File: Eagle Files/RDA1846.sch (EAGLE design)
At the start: 1 part

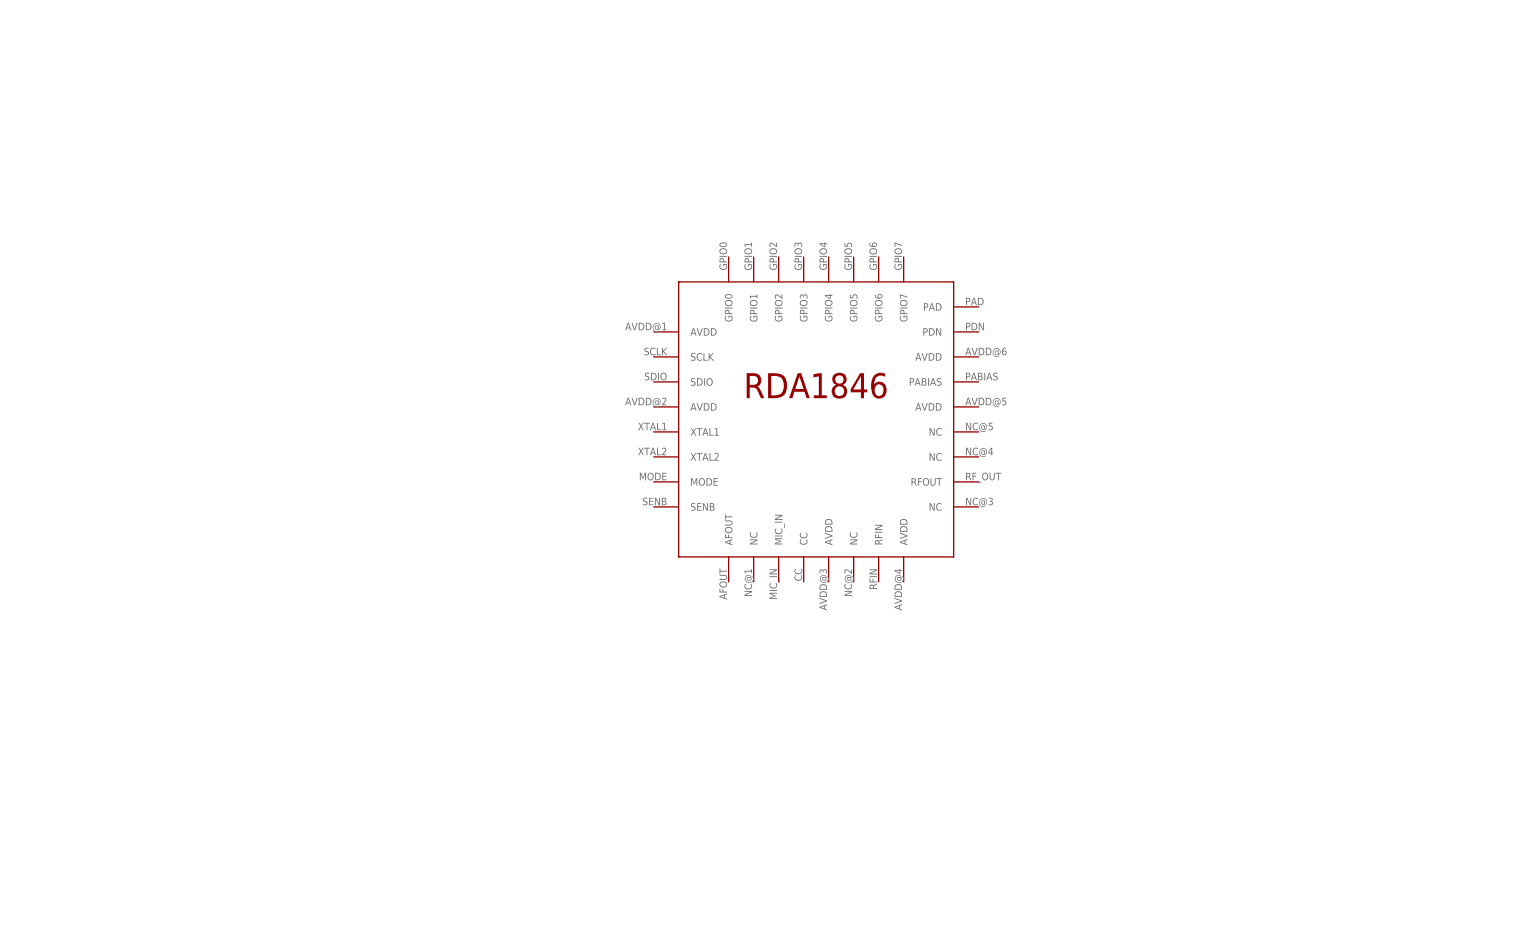
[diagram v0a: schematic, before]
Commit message: Added FA-128 XTAL Library. WIP : Schematic
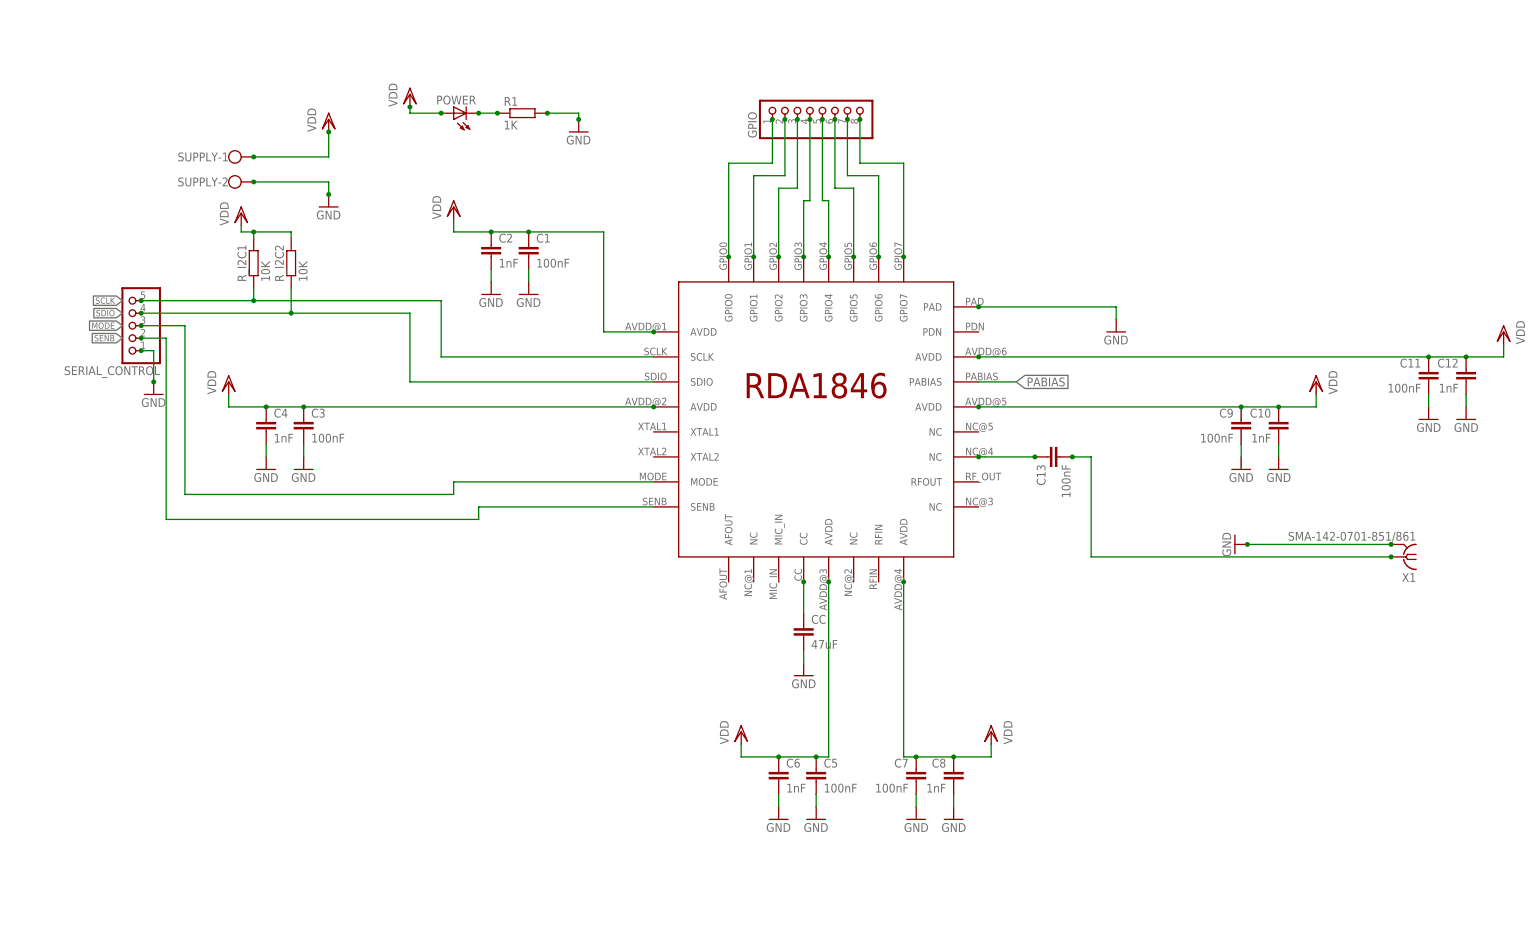
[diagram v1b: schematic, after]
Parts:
- added C1, C11, C13, C3, C5, C7, C9: 100nF, rcl:C-EUC0805
- added C10, C12, C2, C4, C6, C8: 1nF, rcl:C-EUC0805
- added CC: 47uF, rcl:C-EUC0805
- added GPIO: (no value), adafruit:PINHD-1X8CLEANBIG
- added POWER: (no value), adafruit:LEDCHIPLED_1206
- added R1: 1K, rcl:R-EU_R0805
- added R_I2C1, R_I2C2: 10K, rcl:R-EU_R0805
- added SERIAL_CONTROL: (no value), pinhead:PINHD-1X5
- added SUPPLY: (no value), con-wago-500:W237-102
- added X1: SMA-142-0701-851/861, con-coax:SMA-142-0701-851/861
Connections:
- new net GND: C1.2, C10.2, C11.2, C12.2, C2.2, C3.2, C4.2, C5.2, C6.2, C7.2, C8.2, C9.2, CC.2, R1.2, SERIAL_CONTROL.1, SUPPLY-2.KL, U$1.PAD, X1.2
- new net MODE: SERIAL_CONTROL.3, U$1.MODE
- new net N$1: GPIO.1, U$1.GPIO0
- new net N$10: CC.1, U$1.CC
- new net N$11: C13.1, U$1.NC@4
- new net N$12: C13.2, X1.1
- new net N$2: GPIO.8, U$1.GPIO7
- new net N$3: GPIO.2, U$1.GPIO1
- new net N$4: GPIO.7, U$1.GPIO6
- new net N$5: GPIO.3, U$1.GPIO2
- new net N$6: GPIO.6, U$1.GPIO5
- new net N$7: GPIO.4, U$1.GPIO3
- new net N$8: GPIO.5, U$1.GPIO4
- new net N$9: POWER.C, R1.1
- new net PABIAS: U$1.PABIAS
- new net SCLK: R_I2C1.1, SERIAL_CONTROL.5, U$1.SCLK
- new net SDIO: R_I2C2.1, SERIAL_CONTROL.4, U$1.SDIO
- new net SENB: SERIAL_CONTROL.2, U$1.SENB
- new net VDD: C1.1, C10.1, C11.1, C12.1, C2.1, C3.1, C4.1, C5.1, C6.1, C7.1, C8.1, C9.1, POWER.A, R_I2C1.2, R_I2C2.2, SUPPLY-1.KL, U$1.AVDD@1, U$1.AVDD@2, U$1.AVDD@3, U$1.AVDD@4, U$1.AVDD@5, U$1.AVDD@6

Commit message: Schematics done. Layout WIP. Check RF Switch dimensions
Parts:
- added AOUT, MIC: (no value), pinhead:PINHD-1X2
- added C14, C15: 9pF, rcl:C-EUC0805
- added C16, C17: 47uF, rcl:C-EUC0805
- added C18, C19, C20: (no value), rcl:C-USC1206
- added ENABLE, RF_SWITCH: (no value), pinhead:PINHD-1X3
- added PABIAS: (no value), con-wago-500:W237-102
- added RFIN, RFOUT: SMA-142-0701-851/861, con-coax:SMA-142-0701-851/861
- added U$2: CRYSTAL_FA_128, FA_128:CRYSTAL_FA_128
- added U$3: RF_SWITCH, RF_SWITCH:RF_SWITCH
- added X2, X3: SMA-142-0701-871/876, con-coax:SMA-142-0701-871/876
- X1: value SMA-142-0701-851/861 -> SMA-142-0701-871/876; device con-coax:SMA-142-0701-851/861 -> con-coax:SMA-142-0701-871/876
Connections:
- new net N$13: C15.1, U$1.XTAL1, U$2.OP1
- new net N$14: C14.1, U$1.XTAL2, U$2.OP2
- new net N$15: C16.2, U$1.AFOUT
- new net N$16: C17.2, U$1.MIC_IN
- new net N$17: AOUT.2, C16.1
- new net N$18: C17.1, MIC.2
- new net N$19: RFIN.1, U$1.RFIN
- new net N$20: C19.2, X1.1
- new net N$21: C19.1, U$3.J3
- new net N$22: C20.1, U$3.J2
- new net N$23: C20.2, X2.1
- new net N$24: C18.1, U$3.RF
- new net N$25: C18.2, X3.1
- new net N$26: RF_SWITCH.2, U$3.V2
- new net N$27: RF_SWITCH.3, U$3.V1
- new net PDN: ENABLE.2, U$1.PDN
- net GND: now also AOUT.1, C14.2, C15.2, ENABLE.1, MIC.1, PABIAS-2.KL, RFIN.2, RFOUT.2, RF_SWITCH.1, U$2.GND, U$2.GND_1, U$3.GND, X2.2
- net N$11: now also U$1.RFOUT; no longer U$1.NC@4
- net N$12: now also RFOUT.1; no longer X1.1
- net PABIAS: now also PABIAS-1.KL
- net VDD: now also ENABLE.3

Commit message: Placing of component done. Removed demod spec due to size constraints
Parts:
- removed AOUT: (no value), pinhead:PINHD-1X2
- removed C16: 47uF, rcl:C-EUC0805
- removed PABIAS: (no value), con-wago-500:W237-102
- removed RFIN: SMA-142-0701-851/861, con-coax:SMA-142-0701-851/861
- removed RF_SWITCH: (no value), pinhead:PINHD-1X3
- removed SERIAL_CONTROL: (no value), pinhead:PINHD-1X5
- added JP1: (no value), pinhead:PINHD-1X2
- added JP2, JP3: (no value), pinhead:PINHD-1X3
- added JP4, JP5, JP6: (no value), pinhead:PINHD-1X1
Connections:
- removed net N$15: C16.2, U$1.AFOUT
- removed net N$17: AOUT.2, C16.1
- removed net N$19: RFIN.1, U$1.RFIN
- net GND: now also JP1.1, JP2.1, JP3.1, JP4.1, SUPPLY-1.KL; no longer AOUT.1, PABIAS-2.KL, RFIN.2, RF_SWITCH.1, SERIAL_CONTROL.1, SUPPLY-2.KL
- net MODE: now also JP3.3; no longer SERIAL_CONTROL.3
- net N$26: now also JP5.1; no longer RF_SWITCH.2
- net N$27: now also JP6.1; no longer RF_SWITCH.3
- net PABIAS: now also JP1.2; no longer PABIAS-1.KL
- net SCLK: now also JP2.3; no longer SERIAL_CONTROL.5
- net SDIO: now also JP2.2; no longer SERIAL_CONTROL.4
- net SENB: now also JP3.2; no longer SERIAL_CONTROL.2
- net VDD: now also SUPPLY-2.KL; no longer SUPPLY-1.KL

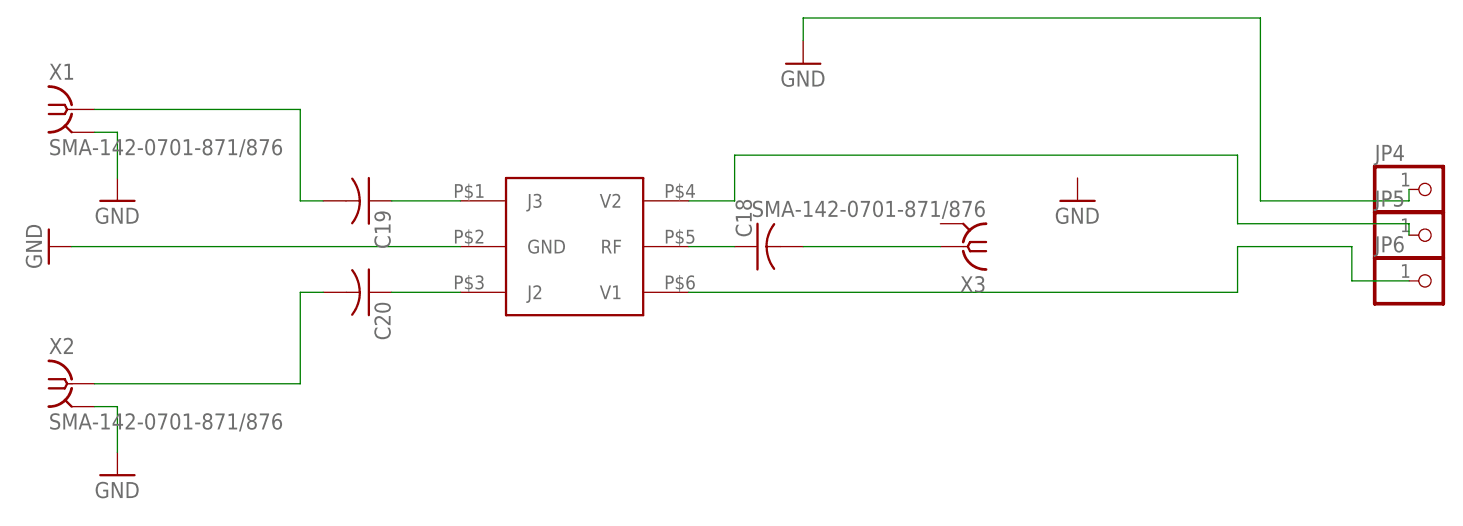
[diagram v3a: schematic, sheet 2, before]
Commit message: Layout RDA almost done. VCC lines remaining
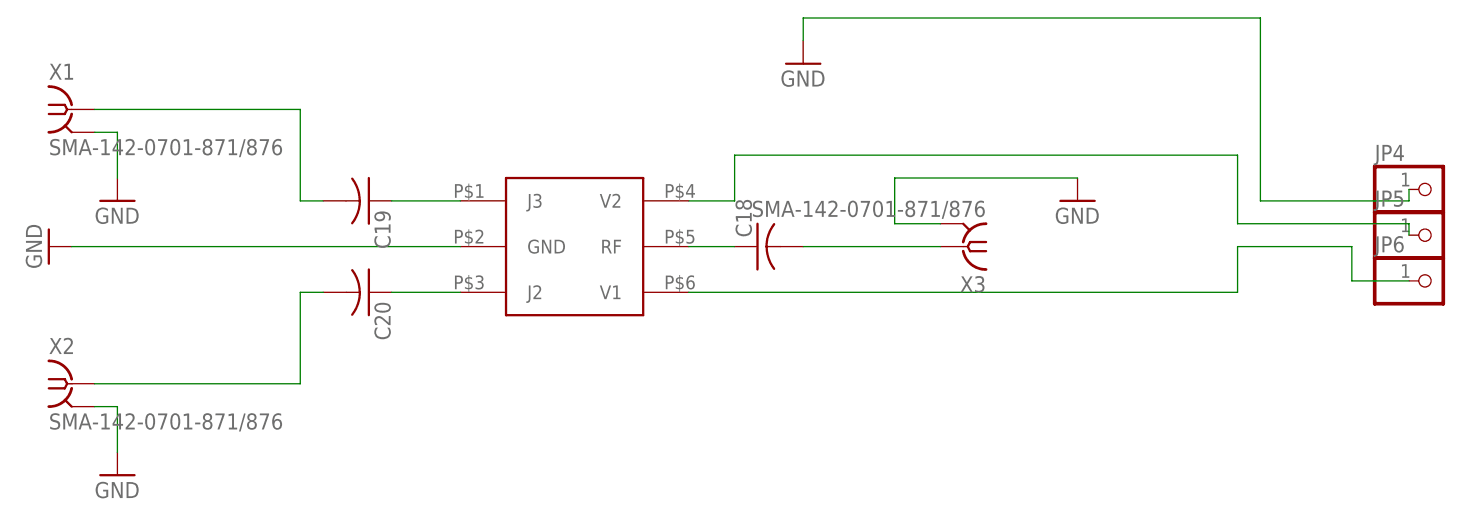
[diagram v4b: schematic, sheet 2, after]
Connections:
- net GND: now also X3.2
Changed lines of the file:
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@@
 <setting verticaltext="up"/>
 </settings>
-<grid distance="50" unitdist="mil" unit="mil" style="lines" multiple="1" display="no" altdistance="0.01" altunitdist="inch" altunit="inch"/>
+<grid distance="0.1" unitdist="inch" unit="inch" style="lines" multiple="1" display="no" altdistance="0.01" altunitdist="inch" altunit="inch"/>
 <layers>
 <layer number="1" name="Top" color="4" fill="1" visible="no" active="no"/>
@@
 <wire x1="156.21" y1="63.5" x2="156.21" y2="64.77" width="0.1524" layer="91"/>
 </segment>
-</net>
+<segment>
+<pinref part="X3" gate="G1" pin="2"/>
+<wire x1="104.14" y1="60.96" x2="99.06" y2="60.96" width="0.1524" layer="91"/>
+<wire x1="99.06" y1="60.96" x2="99.06" y2="66.04" width="0.1524" layer="91"/>
+<pinref part="GND31" gate="1" pin="GND"/>
+<wire x1="99.06" y1="66.04" x2="119.38" y2="66.04" width="0.1524" layer="91"/>
+</segment>
+</net>

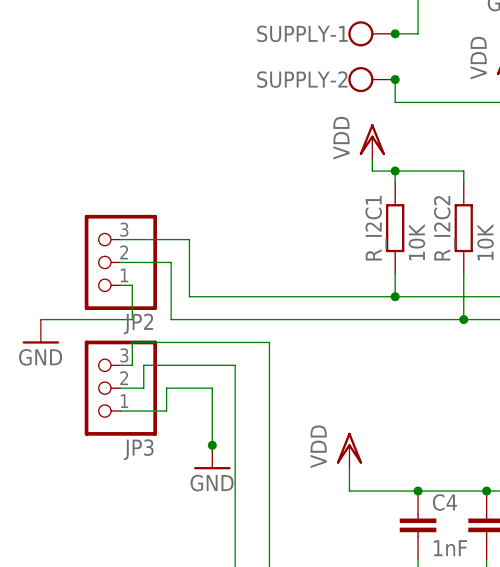
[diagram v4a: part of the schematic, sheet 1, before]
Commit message: Completed layout and routing. Need to adjust labels and values
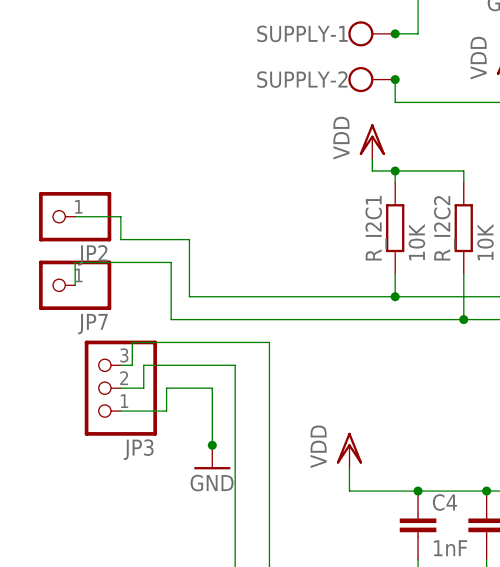
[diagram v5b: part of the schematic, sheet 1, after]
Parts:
- added JP7: (no value), adafruit:PINHD-1X1
- JP2: device pinhead:PINHD-1X3 -> adafruit:PINHD-1X1
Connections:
- net GND: no longer JP2.1
- net SCLK: now also JP2.1; no longer JP2.3
- net SDIO: now also JP7.1; no longer JP2.2
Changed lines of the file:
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@@
 <part name="GND31" library="supply1" deviceset="GND" device=""/>
 <part name="GND32" library="supply1" deviceset="GND" device=""/>
-<part name="JP2" library="pinhead" deviceset="PINHD-1X3" device=""/>
 <part name="JP3" library="pinhead" deviceset="PINHD-1X3" device=""/>
-<part name="GND33" library="supply1" deviceset="GND" device=""/>
 <part name="JP1" library="pinhead" deviceset="PINHD-1X2" device=""/>
 <part name="JP4" library="pinhead" deviceset="PINHD-1X1" device=""/>
 <part name="JP5" library="pinhead" deviceset="PINHD-1X1" device=""/>
 <part name="JP6" library="pinhead" deviceset="PINHD-1X1" device=""/>
+<part name="JP2" library="adafruit" deviceset="PINHD-1X1" device=""/>
+<part name="JP7" library="adafruit" deviceset="PINHD-1X1" device=""/>
 </parts>
 <sheets>
@@
 <instance part="GND26" gate="1" x="62.23" y="113.03"/>
 <instance part="VDD10" gate="G$1" x="62.23" y="128.27" rot="MR0"/>
-<instance part="JP2" gate="A" x="-132.08" y="76.2" rot="R180"/>
 <instance part="JP3" gate="A" x="-132.08" y="62.23" rot="R180"/>
-<instance part="GND33" gate="1" x="-138.43" y="67.31"/>
 <instance part="JP1" gate="G$1" x="68.58" y="97.79" rot="R180"/>
+<instance part="JP2" gate="G$1" x="-137.16" y="81.28" rot="R180"/>
+<instance part="JP7" gate="G$1" x="-137.16" y="73.66" rot="R180"/>
 </instances>
 <busses>
@@
 <junction x="-99.06" y="101.6"/>
 </segment>
-<segment>
-<pinref part="JP2" gate="A" pin="1"/>
-<wire x1="-129.54" y1="73.66" x2="-128.27" y2="73.66" width="0.1524" layer="91"/>
-<wire x1="-128.27" y1="73.66" x2="-128.27" y2="69.85" width="0.1524" layer="91"/>
-<pinref part="GND33" gate="1" pin="GND"/>
-<wire x1="-128.27" y1="69.85" x2="-138.43" y2="69.85" width="0.1524" layer="91"/>
-</segment>
 </net>
 <net name="PABIAS" class="0">
@@
 <junction x="-99.06" y="72.39"/>
 <wire x1="-121.92" y1="72.39" x2="-99.06" y2="72.39" width="0.1524" layer="91"/>
-<pinref part="JP2" gate="A" pin="3"/>
 <wire x1="-129.54" y1="78.74" x2="-121.92" y2="78.74" width="0.1524" layer="91"/>
 <wire x1="-121.92" y1="78.74" x2="-121.92" y2="72.39" width="0.1524" layer="91"/>
+<pinref part="JP2" gate="G$1" pin="1"/>
+<wire x1="-134.62" y1="81.28" x2="-129.54" y2="81.28" width="0.1524" layer="91"/>
+<wire x1="-129.54" y1="81.28" x2="-129.54" y2="78.74" width="0.1524" layer="91"/>
 </segment>
 </net>
@@
 <wire x1="-91.44" y1="74.93" x2="-91.44" y2="69.85" width="0.1524" layer="91"/>
 <junction x="-91.44" y="69.85"/>
-<pinref part="JP2" gate="A" pin="2"/>
-<wire x1="-129.54" y1="76.2" x2="-123.952" y2="76.2" width="0.1524" layer="91"/>
+<wire x1="-134.62" y1="76.2" x2="-123.952" y2="76.2" width="0.1524" layer="91"/>
 <wire x1="-123.952" y1="76.2" x2="-123.952" y2="69.85" width="0.1524" layer="91"/>
-</segment>
-</net>
+<pinref part="JP7" gate="G$1" pin="1"/>
+<wire x1="-134.62" y1="76.2" x2="-134.62" y2="73.66" width="0.1524" layer="91"/>
+</segment>
+</net>
